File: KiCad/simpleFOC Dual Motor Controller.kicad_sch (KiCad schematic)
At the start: 25 parts, among them J101 Conn_01x04, J102 USB_C_Receptacle_USB2.0_14P, J103 Conn_01x06, J104 Conn_01x06, SW101 TS-1088-AR02016, U101 XC6206P332MR, U102 XT60H-M, U103 ESP32-S3-WROOM-1, U104 H5VND5UB

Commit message: finished iteration 1
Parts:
- removed D102, D107: B16WS_C7420327, easyeda2kicad:SOD-323_L1.7-W1.3-LS2.5-FD, symbol easyeda2kicad:B16WS_C7420327
- removed D105, D106: H5VL06B, easyeda2kicad:X3-DFN0603-2_L0.6-W0.3-BI, symbol easyeda2kicad:H5VL06B
- removed J102: USB_C_Receptacle_USB2.0_14P, Connector_USB:USB_C_Receptacle_HCTL_HC-TYPE-C-16P-01A, symbol Connector:USB_C_Receptacle_USB2.0_14P
- removed U102: XT60H-M, easyeda2kicad:CONN-TH_XT60H-M, symbol easyeda2kicad:XT60H-M
- removed U103: ESP32-S3-WROOM-1, RF_Module:ESP32-S3-WROOM-1, symbol RF_Module:ESP32-S3-WROOM-1
- added C106, C107, C113: 100n, Capacitor_SMD:C_0402_1005Metric, symbol Device:C_Small
- added C112, C114: 1u, Capacitor_SMD:C_0402_1005Metric, symbol Device:C_Small
- added C115: 4.7u, Capacitor_SMD:C_0402_1005Metric, symbol Device:C_Small
- added C116: 220n, Capacitor_SMD:C_0402_1005Metric, symbol Device:C_Small
- added CN101: XT60PB-F.G.Y, easyeda2kicad:CONN-TH_XT60PB-F.G.Y, symbol easyeda2kicad:XT60PB-F.G.Y
- added D102, D104, D107: 1N5819WS, Diode_SMD:D_SOD-323, symbol Diode:1N5819WS
- added D103, D105: H5VL10B, easyeda2kicad:SOD-882_L1.0-W0.6-BI, symbol easyeda2kicad:H5VL10B
- added D106: LED, LED_SMD:LED_0603_1608Metric, symbol Device:LED
- added H101, H102, H103, H104, H107: MountingHole, easyeda2kicad:JLC_Tooling_Hole, symbol Mechanical:MountingHole
- added H105, H106: MountingHole, MountingHole:MountingHole_2.2mm_M2, symbol Mechanical:MountingHole
- added J105: USB-TYPE-C-019, easyeda2kicad:TYPE-C-SMD_HX-TYPE-C-16PIN, symbol easyeda2kicad:USB-TYPE-C-019
- added Q101: AO3400A, easyeda2kicad:SOT-23-3_L2.9-W1.3-P1.90-LS2.4-BR, symbol easyeda2kicad:AO3400A
- added R112: 100k, Resistor_SMD:R_0402_1005Metric, symbol Device:R_Small
- added R113: 3.3k, PCM_SparkFun-Resistor:R_0402_1005Metric, symbol Device:R_Small
- added R114: 330, Resistor_SMD:R_0402_1005Metric, symbol Device:R_Small
- added SW102: TS-1088-AR02016, easyeda2kicad:SW-SMD_L3.9-W3.0-P4.45, symbol easyeda2kicad:TS-1088-AR02016
- added U103: STM32G474CBTx, Package_QFP:LQFP-48_7x7mm_P0.5mm, symbol MCU_ST_STM32G4:STM32G474CBTx
- C102: footprint (none) -> Capacitor_SMD:C_0402_1005Metric
- C104: value 22u -> 100n; footprint Capacitor_SMD:C_0603_1608Metric -> Capacitor_SMD:C_0402_1005Metric
- C111: value 1u -> 10n
- R109: value 10k -> 3.3k
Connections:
- net +3.3V: now also C106.1, C107.1, C112.1, C115.1, R114.1, SW102.1, U103.1 (VBAT), U103.21 (VDDA), U103.24 (VDD), U103.36 (VDD), U103.48 (VDD); no longer R109.1
- net +5V: now also D102.1 (K), D107.1 (K)
- net CAL1: now also U103.11 (PA3)
- net CAL2: now also U103.25 (PB11)
- net CHA1: now also U103.30 (PA8)
- net CHA2: now also U103.40 (PB3)
- net CHB1: now also U103.16 (PB0)
- net CHB2: now also U103.41 (PB4)
- net CHC1: now also U103.32 (PA10)
- net CHC2: now also U103.46 (PB9)
- net D+: now also D103.2 (A), J105.A6 (D+), J105.B6 (D+), U103.34 (PA12)
- net D-: now also D105.2 (A), J105.A7 (D-), J105.B7 (D-), U103.33 (PA11)
- net EN1: now also U103.12 (PA4)
- net EN2: now also U103.27 (PB13)
- net FAULT1: now also U103.3 (PC14)
- net FAULT2: now also U103.39 (PA15)
- net GAIN1: now also U103.4 (PC15)
- net GAIN2: now also U103.42 (PB5)
- net GND: now also J101.1 (Pin_1), SW101.1, C106.2, C107.2, C112.2, C113.2, C114.2, C115.2, C116.2, CN101.-, D103.1 (C), D105.1 (C), D106.1 (K), J105.17 (SHIELD), J105.A12B1 (GND), J105.B12A1 (GND), Q101.2 (S), R112.1, U103.19 (VSSA), U103.23 (VSS), U103.35 (VSS), U103.47 (VSS); no longer J101.3 (Pin_3), SW101.2
- net M+: now also CN101.+
- net ctrl_scl: now also J101.4 (Pin_4), U103.37 (PA13); no longer J101.1 (Pin_1)
- net ctrl_sda: now also J101.3 (Pin_3), U103.38 (PA14); no longer J101.2 (Pin_2)
- net snsA1: now also U103.8 (PA0)
- net snsA2: now also U103.28 (PB14)
- net snsB1: now also U103.9 (PA1)
- net snsB2: now also U103.26 (PB12)
- net snsC1: now also U103.10 (PA2)
- net snsC2: now also U103.29 (PB15)
- net sns_cs1: now also U103.22 (PB10)
- net sns_cs2: now also U103.18 (PB2)
- net sns_miso: now also U103.14 (PA6)
- net sns_mosi: now also U103.15 (PA7)
- net sns_sck: now also U103.13 (PA5)
- net ~{rst}: now also SW101.2, Q101.3 (D), U103.7 (PG10); no longer R109.2, SW101.1
- net at R108.1: now also J105.B5 (CC2)
- net at R107.1: now also J105.A5 (CC1)
- new net: C116.1, D104.1 (K), R109.2
- new net: D104.2 (A), Q101.1 (G), R112.2, R113.1
- new net: D102.2 (A), J105.A9B4 (VBUS), J105.B9A4 (VBUS)
- new net: R113.2, SW102.2
- new net: D106.2 (A), R114.2
- new net: D107.2 (A), J101.2 (Pin_2)
- new net CHLA1: U103.2 (PC13)
- new net CHLA2: U103.43 (PB6)
- new net CHLB1: U103.31 (PA9)
- new net CHLB2: R109.1, U103.45 (PB8)
- new net CHLC1: U103.5 (PF0)
- new net CHLC2: U103.17 (PB1)
- new net VREF: C113.1, C114.1, U103.20 (VREF+)
- no-connect marks 0 -> 2
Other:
- sheet Motor Driver 1 ports: added INLA, INLB, INLC, VREF; removed ~{HI-Z}
- sheet Motor Driver 2 ports: added INLA, INLB, INLC, VREF; removed ~{HI-Z}
- note added: "*Note* Top = RST+DFU mode Bottom = RST"
- moved on the sheet: C101, C102, C111, D101, R107, R108, SW101

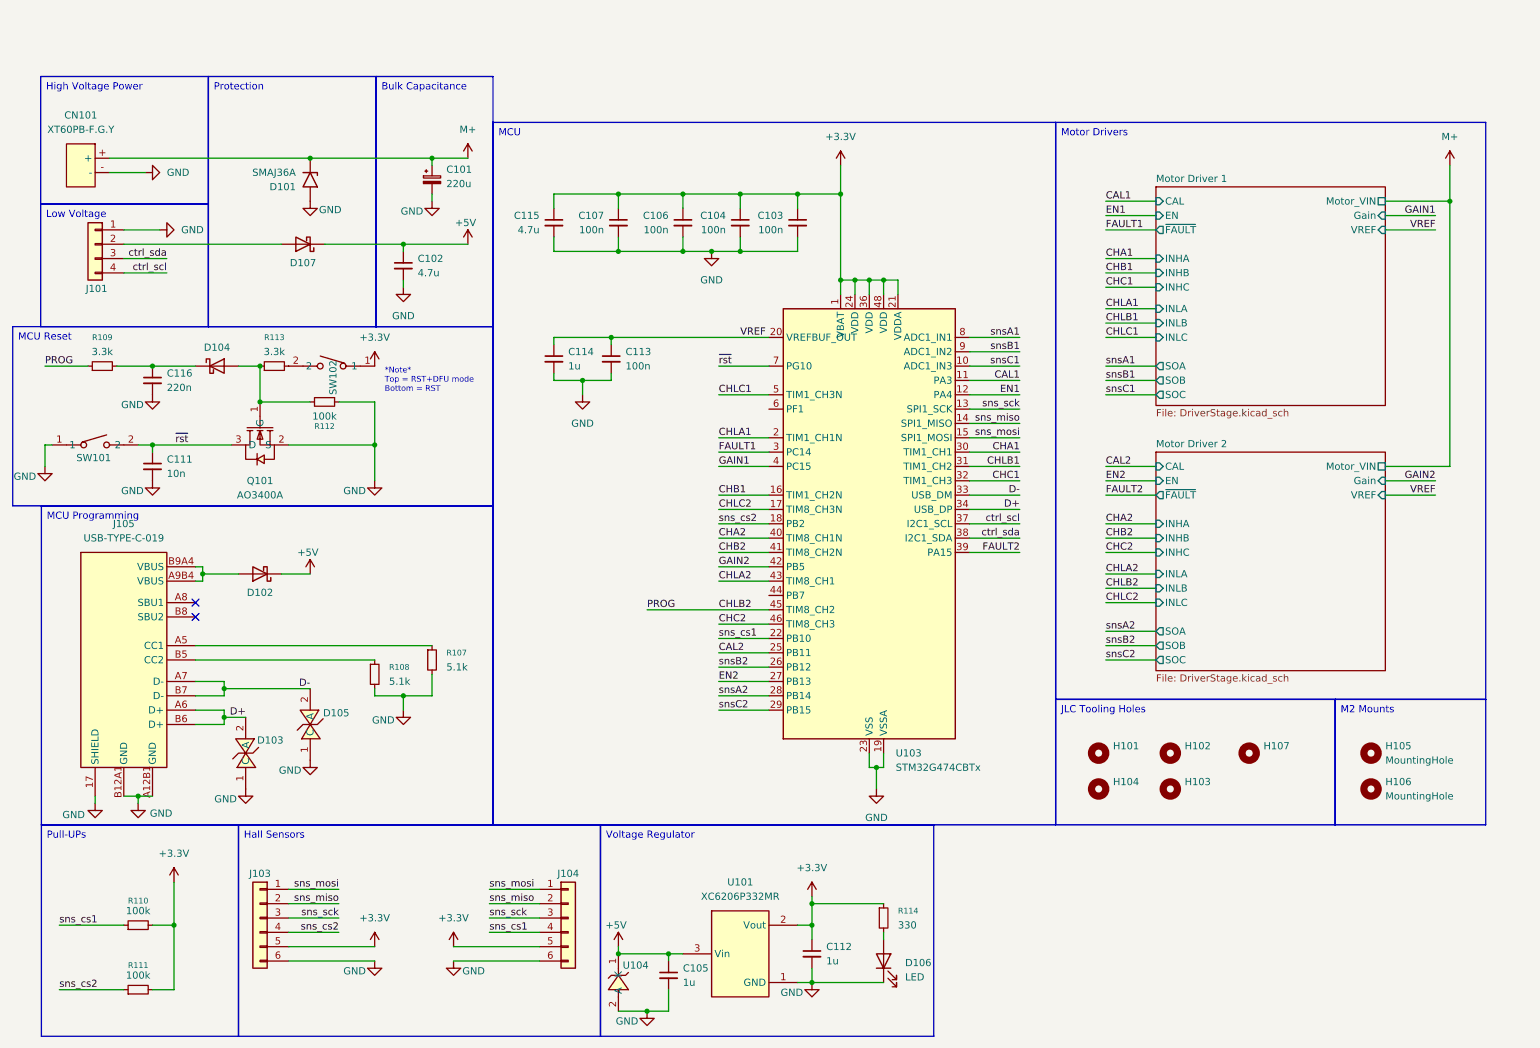
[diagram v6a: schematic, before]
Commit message: added bulk ceramic capacitance
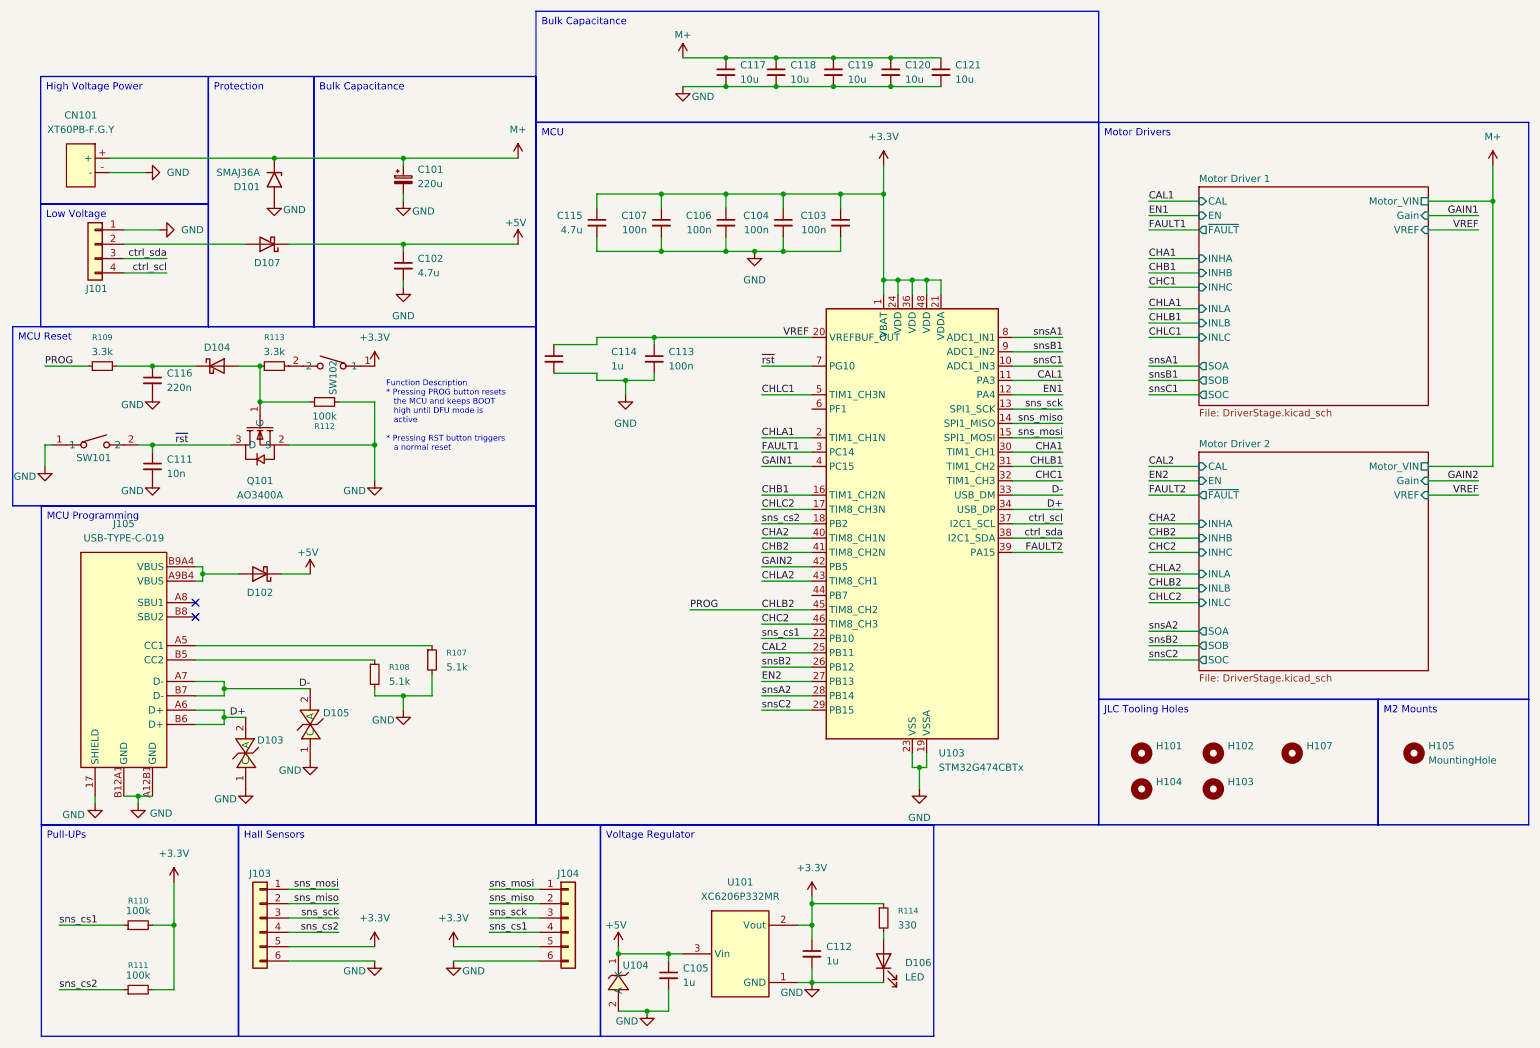
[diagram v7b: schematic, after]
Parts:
- removed H106: MountingHole, MountingHole:MountingHole_2.2mm_M2, symbol Mechanical:MountingHole
- added C117, C118, C119, C120, C121: 10u, Capacitor_SMD:C_1206_3216Metric, symbol Device:C_Small
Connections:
- net GND: now also C117.2, C118.2, C119.2, C120.2, C121.2
- net M+: now also C117.1, C118.1, C119.1, C120.1, C121.1
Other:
- note added: "Function Description * Pressing PROG button resets the MCU and keeps BOOT high until DFU mode is active * Pressing RST button triggers a normal reset"
- note removed: "*Note* Top = RST+DFU mode Bottom = RST"
- moved on the sheet: C101, C103, C104, C106, C107, C113, C115, D101, D107, H101, H102, H103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
